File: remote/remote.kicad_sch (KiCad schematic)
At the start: 31 parts, among them J1 Conn_01x02, J2 Conn_01x04, Q1 Q_NPN_BEC, U1 IRM-H638T, U2 E103-W05, U3 HT66F2390, U4 AMS1117-3.3, Y1 11.0592M

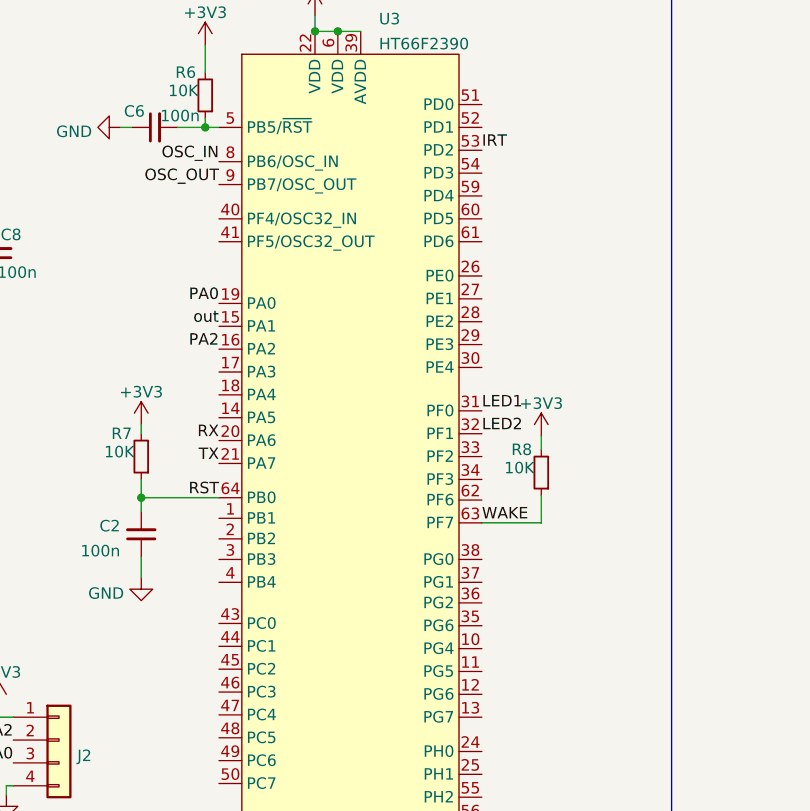
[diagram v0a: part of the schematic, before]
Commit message: add code and finish inferred transmit and receive with NEC
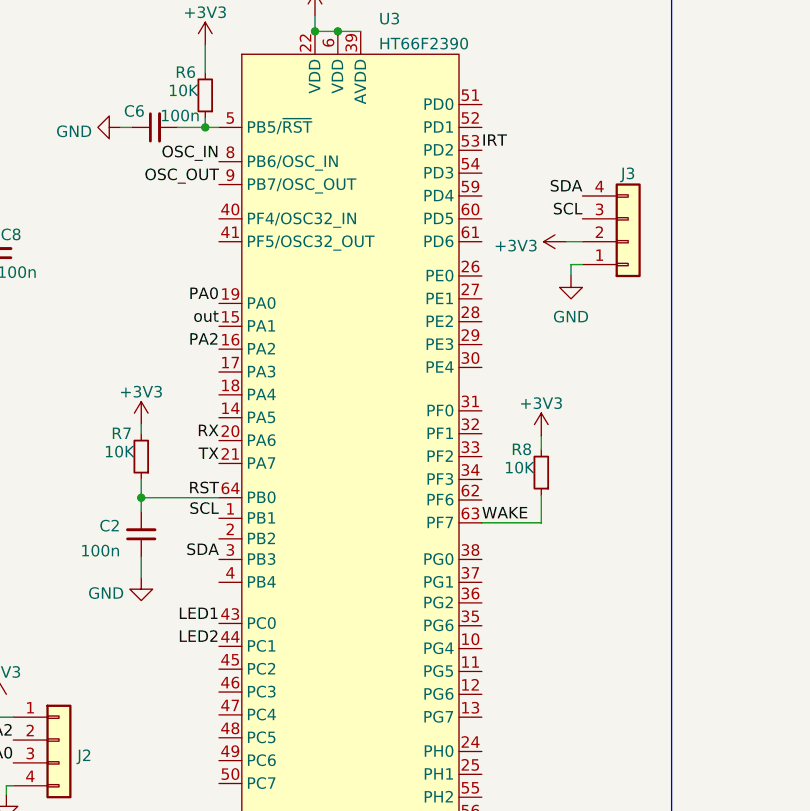
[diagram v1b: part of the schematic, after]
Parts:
- added J3: Conn_01x04, Connector_PinHeader_2.54mm:PinHeader_1x04_P2.54mm_Vertical, symbol Connector_Generic:Conn_01x04
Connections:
- net +3V3: now also J3.2 (Pin_2)
- net GND: now also J3.1 (Pin_1)
- net LED1: now also U3.43 (PC0); no longer U3.31 (PF0)
- net LED2: now also U3.44 (PC1); no longer U3.32 (PF1)
- net SCL: now reaches U3.1 (PB1)
- net SCL: now also J3.3 (Pin_3)
- net SDA: now reaches U3.3 (PB3)
- net SDA: now also J3.4 (Pin_4)
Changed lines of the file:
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@@
+    (stroke (width 0) (type default) (color 0 0 0 0))
+  )
+  (wire (pts (xy 105.664 108.966) (xy 107.442 108.966))
     (stroke (width 0) (type default) (color 0 0 0 0))
   )
@@
     (stroke (width 0) (type default) (color 0 0 0 0))
   )
+  (wire (pts (xy 106.172 111.506) (xy 107.442 111.506))
+    (stroke (width 0) (type default) (color 0 0 0 0))
+  )
   (wire (pts (xy 102.87 130.556) (xy 102.87 132.08))
     (stroke (width 0) (type default) (color 0 0 0 0))
@@
   )
   (wire (pts (xy 56.134 96.266) (xy 57.404 96.266))
+    (stroke (width 0) (type default) (color 0 0 0 0))
+  )
+  (wire (pts (xy 106.172 112.776) (xy 106.172 111.506))
     (stroke (width 0) (type default) (color 0 0 0 0))
   )
@@
     (effects (font (size 1.27 1.27)) (justify right bottom))
   )
+  (label "SCL" (at 67.056 139.7 180)
+    (effects (font (size 1.27 1.27)) (justify right bottom))
+  )
   (label "WAKE" (at 255.27 30.988 180)
     (effects (font (size 1.27 1.27)) (justify right bottom))
@@
     (effects (font (size 1.27 1.27)) (justify right bottom))
   )
-  (label "LED1" (at 96.266 127.762 0)
-    (effects (font (size 1.27 1.27)) (justify left bottom))
+  (label "SCL" (at 107.442 106.426 180)
+    (effects (font (size 1.27 1.27)) (justify right bottom))
+  )
+  (label "LED1" (at 67.056 151.384 180)
+    (effects (font (size 1.27 1.27)) (justify right bottom))
   )
   (label "out" (at 189.23 46.228 0)
@@
     (effects (font (size 1.27 1.27)) (justify right bottom))
   )
+  (label "SDA" (at 67.056 144.272 180)
+    (effects (font (size 1.27 1.27)) (justify right bottom))
+  )
+  (label "SDA" (at 107.442 103.886 180)
+    (effects (font (size 1.27 1.27)) (justify right bottom))
+  )
   (label "RST" (at 67.056 137.414 180)
     (effects (font (size 1.27 1.27)) (justify right bottom))
@@
     (effects (font (size 1.27 1.27)) (justify right bottom))
   )
-  (label "LED2" (at 96.266 130.302 0)
-    (effects (font (size 1.27 1.27)) (justify left bottom))
+  (label "LED2" (at 67.056 153.924 180)
+    (effects (font (size 1.27 1.27)) (justify right bottom))
   )
   (label "IRT" (at 96.266 98.806 0)
@@
     )
     (property "Datasheet" "" (id 3) (at 65.532 87.122 0)
+      (effects (font (size 1.27 1.27)) hide)
+    )
+    (pin "1")
+  )
+  (symbol (lib_id "power:+3V3") (at 105.664 108.966 90) (unit 1)
+    (in_bom yes) (on_board yes) (fields_autoplaced)
+    (property "Reference" "#PWR?" (id 0) (at 109.474 108.966 0)
+      (effects (font (size 1.27 1.27)) hide)
+    )
+    (property "Value" "+3V3" (id 1) (at 102.489 109.445 90)
+      (effects (font (size 1.27 1.27)) (justify left))
+    )
+    (property "Footprint" "" (id 2) (at 105.664 108.966 0)
+      (effects (font (size 1.27 1.27)) hide)
+    )
+    (property "Datasheet" "" (id 3) (at 105.664 108.966 0)
       (effects (font (size 1.27 1.27)) hide)
     )
@@
     )
     (property "Datasheet" "" (id 3) (at 262.89 62.992 0)
+      (effects (font (size 1.27 1.27)) hide)
+    )
+    (pin "1")
+  )
+  (symbol (lib_id "Connector_Generic:Conn_01x04") (at 112.522 108.966 0) (mirror x) (unit 1)
+    (in_bom yes) (on_board yes) (fields_autoplaced)
+    (property "Reference" "J3" (id 0) (at 112.522 101.4245 0))
+    (property "Value" "Conn_01x04" (id 1) (at 114.554 105.8294 0)
+      (effects (font (size 1.27 1.27)) (justify left) hide)
+    )
+    (property "Footprint" "Connector_PinHeader_2.54mm:PinHeader_1x04_P2.54mm_Vertical" (id 2) (at 112.522 108.966 0)
+      (effects (font (size 1.27 1.27)) hide)
+    )
+    (property "Datasheet" "~" (id 3) (at 112.522 108.966 0)
+      (effects (font (size 1.27 1.27)) hide)
+    )
+    (pin "1")
+    (pin "2")
+    (pin "3")
+    (pin "4")
+  )
+  (symbol (lib_id "power:GND") (at 106.172 112.776 0) (unit 1)
+    (in_bom yes) (on_board yes) (fields_autoplaced)
+    (property "Reference" "#PWR0107" (id 0) (at 106.172 119.126 0)
+      (effects (font (size 1.27 1.27)) hide)
+    )
+    (property "Value" "GND" (id 1) (at 106.172 117.3385 0))
+    (property "Footprint" "" (id 2) (at 106.172 112.776 0)
+      (effects (font (size 1.27 1.27)) hide)
+    )
+    (property "Datasheet" "" (id 3) (at 106.172 112.776 0)
       (effects (font (size 1.27 1.27)) hide)
     )
@@
       (reference "#PWR0105") (unit 1) (value "+3V3") (footprint "")
     )
+    (path "/a44f0ea9-6e35-4bb5-a54e-533fdc6788a4"
+      (reference "#PWR0107") (unit 1) (value "GND") (footprint "")
+    )
+    (path "/324dc02f-a95e-4354-b421-f4b8870d075b"
+      (reference "#PWR?") (unit 1) (value "+3V3") (footprint "")
+    )
     (path "/968346de-ae39-4955-adb7-0be7ddec2480"
       (reference "C1") (unit 1) (value "4.7u") (footprint "Capacitor_SMD:C_0603_1608Metric")
@@
       (reference "J2") (unit 1) (value "Conn_01x04") (footprint "Connector_PinHeader_2.54mm:PinHeader_1x04_P2.54mm_Vertical")
     )
+    (path "/a0210d0e-f02a-4337-bb4a-e12adf73e149"
+      (reference "J3") (unit 1) (value "Conn_01x04") (footprint "Connector_PinHeader_2.54mm:PinHeader_1x04_P2.54mm_Vertical")
+    )
     (path "/85310475-60d8-4220-98b6-770c04c2a7c1"
